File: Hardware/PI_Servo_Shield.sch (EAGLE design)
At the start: 109 parts, among them J1 RASPBERRYPI-40-PIN-GPIO, J19 QWIIC, J20 USB C, J21 Serial, Q1 2N7002PW, Q12 2.5A/30V/105mΩ, Q2 2.5A/30V/105mΩ, Q4 2N7002PW, Q5 2.5A/30V/105mΩ, Q7 2.5A/30V/105mΩ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

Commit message: Added tRestrict around standofs as required by HAT specs
Also moved to correct 2.5 A PTC (1812 package).
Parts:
- F2: value 6V/2A -> 16V/2.5A(5A TRIP); device SparkFun-Fuses:PPTC_6V2A -> SparkFun-Fuses:PPTC_16V_2.5A
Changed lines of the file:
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@@
 <grid distance="0.1" unitdist="inch" unit="inch" style="lines" multiple="1" display="no" altdistance="0.01" altunitdist="inch" altunit="inch"/>
 <layers>
-<layer number="1" name="Top" color="4" fill="1" visible="yes" active="no"/>
-<layer number="2" name="Route2" color="1" fill="3" visible="yes" active="no"/>
-<layer number="3" name="Route3" color="4" fill="3" visible="yes" active="no"/>
-<layer number="4" name="Route4" color="1" fill="4" visible="yes" active="no"/>
-<layer number="5" name="Route5" color="4" fill="4" visible="yes" active="no"/>
-<layer number="6" name="Route6" color="1" fill="8" visible="yes" active="no"/>
-<layer number="7" name="Route7" color="4" fill="8" visible="yes" active="no"/>
-<layer number="8" name="Route8" color="1" fill="2" visible="yes" active="no"/>
-<layer number="9" name="Route9" color="4" fill="2" visible="yes" active="no"/>
-<layer number="10" name="Route10" color="1" fill="7" visible="yes" active="no"/>
-<layer number="11" name="Route11" color="4" fill="7" visible="yes" active="no"/>
-<layer number="12" name="Route12" color="1" fill="5" visible="yes" active="no"/>
-<layer number="13" name="Route13" color="4" fill="5" visible="yes" active="no"/>
-<layer number="14" name="Route14" color="1" fill="6" visible="yes" active="no"/>
-<layer number="15" name="Route15" color="4" fill="6" visible="yes" active="no"/>
-<layer number="16" name="Bottom" color="1" fill="1" visible="yes" active="no"/>
-<layer number="17" name="Pads" color="2" fill="1" visible="yes" active="no"/>
-<layer number="18" name="Vias" color="2" fill="1" visible="yes" active="no"/>
-<layer number="19" name="Unrouted" color="6" fill="1" visible="yes" active="no"/>
-<layer number="20" name="Dimension" color="15" fill="1" visible="yes" active="no"/>
-<layer number="21" name="tPlace" color="16" fill="1" visible="yes" active="no"/>
-<layer number="22" name="bPlace" color="14" fill="1" visible="yes" active="no"/>
-<layer number="23" name="tOrigins" color="15" fill="1" visible="yes" active="no"/>
-<layer number="24" name="bOrigins" color="15" fill="1" visible="yes" active="no"/>
-<layer number="25" name="tNames" color="7" fill="1" visible="yes" active="no"/>
-<layer number="26" name="bNames" color="7" fill="1" visible="yes" active="no"/>
-<layer number="27" name="tValues" color="7" fill="1" visible="yes" active="no"/>
-<layer number="28" name="bValues" color="7" fill="1" visible="yes" active="no"/>
+<layer number="1" name="Top" color="4" fill="1" visible="no" active="no"/>
+<layer number="2" name="Route2" color="1" fill="3" visible="no" active="no"/>
+<layer number="3" name="Route3" color="4" fill="3" visible="no" active="no"/>
+<layer number="4" name="Route4" color="1" fill="4" visible="no" active="no"/>
+<layer number="5" name="Route5" color="4" fill="4" visible="no" active="no"/>
+<layer number="6" name="Route6" color="1" fill="8" visible="no" active="no"/>
+<layer number="7" name="Route7" color="4" fill="8" visible="no" active="no"/>
+<layer number="8" name="Route8" color="1" fill="2" visible="no" active="no"/>
+<layer number="9" name="Route9" color="4" fill="2" visible="no" active="no"/>
+<layer number="10" name="Route10" color="1" fill="7" visible="no" active="no"/>
+<layer number="11" name="Route11" color="4" fill="7" visible="no" active="no"/>
+<layer number="12" name="Route12" color="1" fill="5" visible="no" active="no"/>
+<layer number="13" name="Route13" color="4" fill="5" visible="no" active="no"/>
+<layer number="14" name="Route14" color="1" fill="6" visible="no" active="no"/>
+<layer number="15" name="Route15" color="4" fill="6" visible="no" active="no"/>
+<layer number="16" name="Bottom" color="1" fill="1" visible="no" active="no"/>
+<layer number="17" name="Pads" color="2" fill="1" visible="no" active="no"/>
+<layer number="18" name="Vias" color="2" fill="1" visible="no" active="no"/>
+<layer number="19" name="Unrouted" color="6" fill="1" visible="no" active="no"/>
+<layer number="20" name="Dimension" color="15" fill="1" visible="no" active="no"/>
+<layer number="21" name="tPlace" color="16" fill="1" visible="no" active="no"/>
+<layer number="22" name="bPlace" color="14" fill="1" visible="no" active="no"/>
+<layer number="23" name="tOrigins" color="15" fill="1" visible="no" active="no"/>
+<layer number="24" name="bOrigins" color="15" fill="1" visible="no" active="no"/>
+<layer number="25" name="tNames" color="7" fill="1" visible="no" active="no"/>
+<layer number="26" name="bNames" color="7" fill="1" visible="no" active="no"/>
+<layer number="27" name="tValues" color="7" fill="1" visible="no" active="no"/>
+<layer number="28" name="bValues" color="7" fill="1" visible="no" active="no"/>
 <layer number="29" name="tStop" color="7" fill="3" visible="no" active="no"/>
 <layer number="30" name="bStop" color="7" fill="6" visible="no" active="no"/>
@@
 <layer number="35" name="tGlue" color="7" fill="4" visible="no" active="no"/>
 <layer number="36" name="bGlue" color="7" fill="5" visible="no" active="no"/>
-<layer number="37" name="tTest" color="7" fill="1" visible="yes" active="no"/>
-<layer number="38" name="bTest" color="7" fill="1" visible="yes" active="no"/>
+<layer number="37" name="tTest" color="7" fill="1" visible="no" active="no"/>
+<layer number="38" name="bTest" color="7" fill="1" visible="no" active="no"/>
 <layer number="39" name="tKeepout" color="4" fill="11" visible="no" active="no"/>
 <layer number="40" name="bKeepout" color="1" fill="11" visible="no" active="no"/>
@@
 <layer number="44" name="Drills" color="7" fill="1" visible="no" active="no"/>
 <layer number="45" name="Holes" color="7" fill="1" visible="no" active="no"/>
-<layer number="46" name="Milling" color="3" fill="1" visible="yes" active="no"/>
-<layer number="47" name="Measures" color="7" fill="1" visible="yes" active="no"/>
-<layer number="48" name="Document" color="62" fill="7" visible="yes" active="no"/>
-<layer number="49" name="Reference" color="7" fill="1" visible="yes" active="no"/>
-<layer number="50" name="dxf" color="7" fill="1" visible="yes" active="no"/>
-<layer number="51" name="tDocu" color="6" fill="1" visible="yes" active="no"/>
-<layer number="52" name="bDocu" color="7" fill="1" visible="yes" active="no"/>
-<layer number="53" name="tGND_GNDA" color="7" fill="9" visible="yes" active="no"/>
-<layer number="54" name="bGND_GNDA" color="1" fill="9" visible="yes" active="no"/>
-<layer number="56" name="wert" color="7" fill="1" visible="yes" active="no"/>
-<layer number="57" name="tCAD" color="7" fill="1" visible="yes" active="no"/>
-<layer number="59" name="tCarbon" color="7" fill="1" visible="yes" active="no"/>
-<layer number="60" name="bCarbon" color="7" fill="1" visible="yes" active="no"/>
+<layer number="46" name="Milling" color="3" fill="1" visible="no" active="no"/>
+<layer number="47" name="Measures" color="7" fill="1" visible="no" active="no"/>
+<layer number="48" name="Document" color="62" fill="7" visible="no" active="no"/>
+<layer number="49" name="Reference" color="7" fill="1" visible="no" active="no"/>
+<layer number="50" name="dxf" color="7" fill="1" visible="no" active="no"/>
+<layer number="51" name="tDocu" color="6" fill="1" visible="no" active="no"/>
+<layer number="52" name="bDocu" color="7" fill="1" visible="no" active="no"/>
+<layer number="53" name="tGND_GNDA" color="7" fill="9" visible="no" active="no"/>
+<layer number="54" name="bGND_GNDA" color="1" fill="9" visible="no" active="no"/>
+<layer number="56" name="wert" color="7" fill="1" visible="no" active="no"/>
+<layer number="57" name="tCAD" color="7" fill="1" visible="no" active="no"/>
+<layer number="59" name="tCarbon" color="7" fill="1" visible="no" active="no"/>
+<layer number="60" name="bCarbon" color="7" fill="1" visible="no" active="no"/>
 <layer number="88" name="SimResults" color="9" fill="1" visible="no" active="yes"/>
 <layer number="89" name="SimProbes" color="9" fill="1" visible="no" active="yes"/>
@@
 <part name="GND16" library="SparkFun-PowerSymbols" deviceset="GND" device=""/>
 <part name="JP2" library="SparkFun-Jumpers" deviceset="JUMPER-SMT_2_NO" device="_SILK" value="FUSE BP"/>
-<part name="F2" library="SparkFun-Fuses" deviceset="PPTC" device="_6V2A" value="6V/2A"/>
+<part name="F2" library="SparkFun-Fuses" deviceset="PPTC" device="_16V_2.5A" value="16V/2.5A(5A TRIP)"/>
 <part name="SUPPLY3" library="SparkFun-PowerSymbols" deviceset="VIN" device="" value="USB-5V"/>
 <part name="GND4" library="SparkFun-PowerSymbols" deviceset="GND" device=""/>

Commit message: final stuff during eng check for reds
Schematic cleanup.
Corrected OR Gate in latest library to correct SOT353 (was from older library)
Added PROD_ID to dual PNP (TRAN-14386)
moved some vias around to avoid cutting into silk.
re-routed some "natural bridges" on bottom parts.
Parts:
- removed U4: 7432SE, SparkFun:7432SE
- added U2: SN74LVC1G32DCKR, SparkFun-IC-Logic:7432
- J21: value Serial -> RVR
- Q1, Q4: value 2N7002PW -> 310mA/60V/1.6Ω
- Q12, Q2, Q5, Q7, Q9: value 2.5A/30V/105mΩ -> 20V/4.2A/52mΩ/1.4W; device SparkFun-DiscreteSemi:MOSFET_PCH-DMG2307L -> SparkFun-DiscreteSemi:MOSFET_PCH-DMG2305UX-7
- R17, R18: value 100 -> 240; device SparkFun-Resistors:100OHM-0603-1/4W-5% -> SparkFun-Resistors:240OHM-0603-1/10W-1%
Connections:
- net GND: now also U2G2.P$V-; no longer U4.GND
- net N$17: now also U2G1.Y; no longer U4.Y
- net PI-5V: now also U2G2.P$V+; no longer U4.VCC
- net RVR-5V: now also U2G1.A; no longer U4.A
- net USB-5V: now also U2G1.B; no longer U4.B
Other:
- note added: "(Isolates Pi 5V header from Servo power when USB OR RVR is connected)"
- note added: "Cut this jumper (JP4) to *permanently* Isolate Pi 5V Header from Servo power"
- note added: "Serial UART 4-pin Header"
- note added: "Test points"
- note added: "v12"
- note removed: "Clear this jumper to disconnect servo power from Pi power rail"
- note removed: "Serial Connector"
- note removed: "v11"
- moved on the sheet: C3, C4, C5, C6, C7, C8, Q11Q1, Q11Q2, Q12, R17, R18, R19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

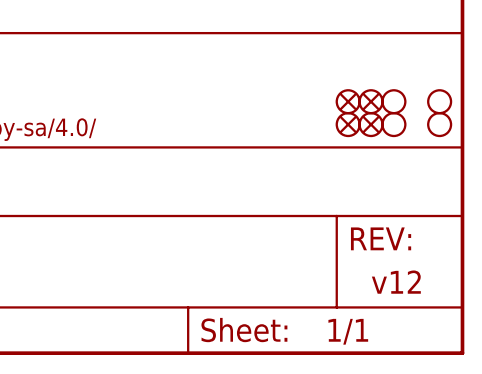
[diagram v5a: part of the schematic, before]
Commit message: qc double-check changes - and SS mods
-bumped version to v20 (was previously v12)
-Moved bottom parts for more clearance from SS route
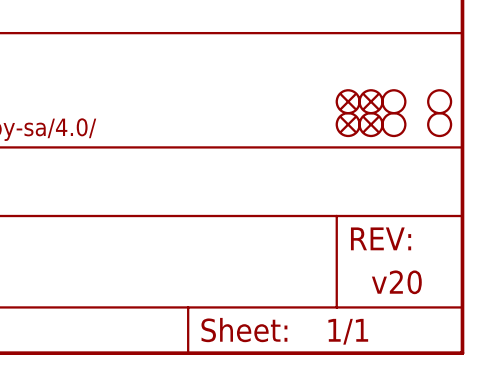
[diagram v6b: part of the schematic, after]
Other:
- note added: "v20"
- note removed: "v12"
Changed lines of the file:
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@@
 <plain>
 <text x="349.758" y="11.43" size="2.54" layer="94" font="vector">M. Hord</text>
-<text x="421.64" y="6.604" size="2.54" layer="94" font="vector" ratio="12">v12</text>
+<text x="421.64" y="6.604" size="2.54" layer="94" font="vector" ratio="12">v20</text>
 <wire x1="0" y1="152.4" x2="139.7" y2="152.4" width="0.3048" layer="97" style="longdash"/>
 <wire x1="139.7" y1="152.4" x2="139.7" y2="0" width="0.3048" layer="97" style="longdash"/>

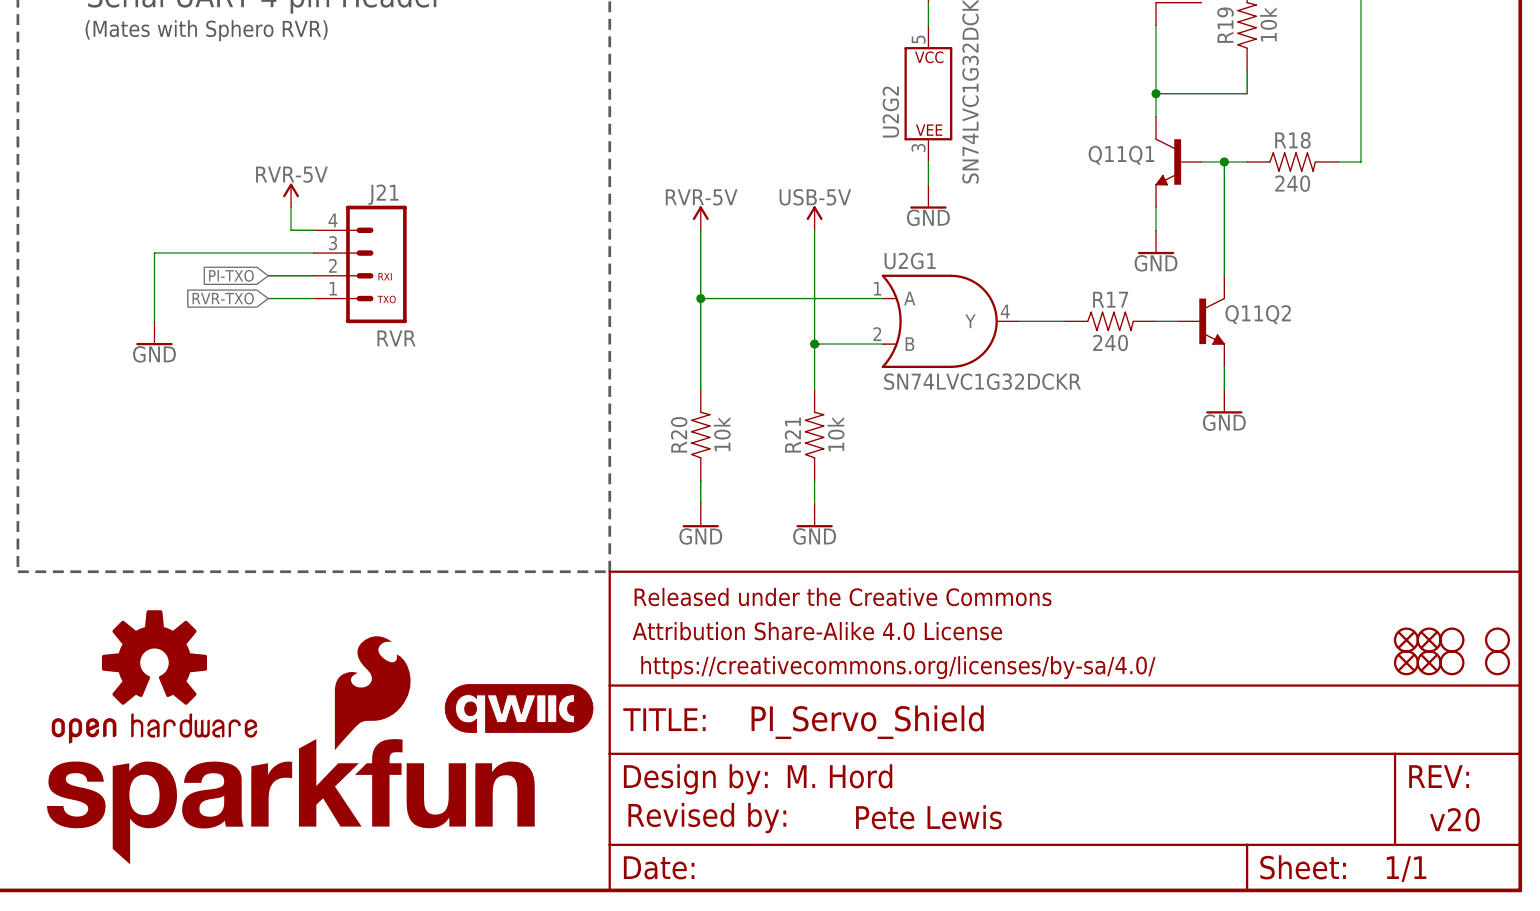
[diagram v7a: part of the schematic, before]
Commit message: Fixed RX/TX on RVR 4-pin header
-swapped rx/tx lines on the RVR header.

-updated board buzzard labels on the header to reflect correction (and note, they are labeled in relation to the raspi)

-bumped version to v21 in brd and sch

-added RVR pin names in schematic next to 4-pin header. Put it on info layer. Just there to clarify what those pins are (in relation to the RVR).

-moved test point (TP23) 0.05 inch east/right to gain more clarance from nearby bottom resistor (R13).
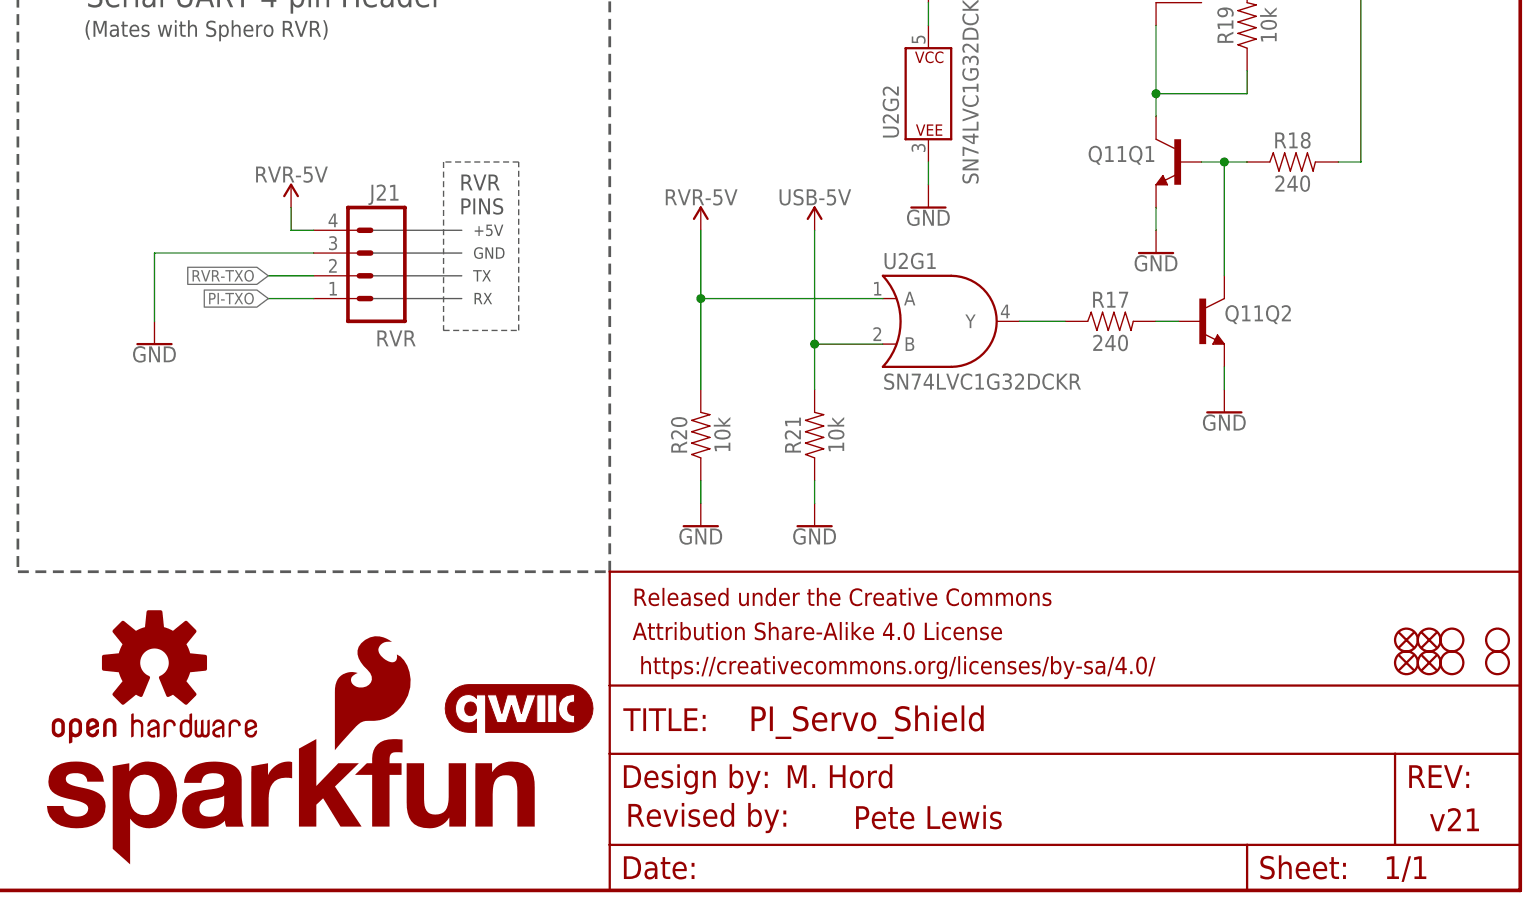
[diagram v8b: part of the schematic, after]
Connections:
- net PI-TXO: now also J21.1; no longer J21.2
- net RVR-TXO: now also J21.2; no longer J21.1
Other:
- note added: "+5V"
- note added: "GND"
- note added: "RVR PINS"
- note added: "RX"
- note added: "TX"
- note added: "v21"
- note removed: "RXI"
- note removed: "TXO"
- note removed: "v20"
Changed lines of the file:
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@@
 <?xml version="1.0" encoding="utf-8"?>
 <!DOCTYPE eagle SYSTEM "eagle.dtd">
-<eagle version="9.2.2">
+<eagle version="9.4.0">
 <drawing>
 <settings>
@@
 <plain>
 <text x="349.758" y="11.43" size="2.54" layer="94" font="vector">M. Hord</text>
-<text x="421.64" y="6.604" size="2.54" layer="94" font="vector" ratio="12">v20</text>
+<text x="421.64" y="6.604" size="2.54" layer="94" font="vector" ratio="12">v21</text>
 <wire x1="0" y1="152.4" x2="139.7" y2="152.4" width="0.3048" layer="97" style="longdash"/>
 <wire x1="139.7" y1="152.4" x2="139.7" y2="0" width="0.3048" layer="97" style="longdash"/>
@@
 <wire x1="381" y1="200.66" x2="419.1" y2="200.66" width="0.3048" layer="97" style="shortdash"/>
 <wire x1="381" y1="139.7" x2="381" y2="200.66" width="0.3048" layer="97" style="shortdash"/>
-<text x="304.292" y="65.532" size="0.8128" layer="94" font="vector">TXO</text>
-<text x="304.292" y="68.072" size="0.8128" layer="94" font="vector">RXI</text>
 <text x="213.36" y="101.6" size="1.778" layer="97" font="vector">Serial Swtich</text>
 <text x="213.36" y="99.568" size="1.778" layer="97" font="vector" align="top-left">Selects which TX source
@@
 <text x="146.05" y="42.418" size="2.54" layer="97" font="vector">Test points</text>
 <wire x1="282.702" y1="242.062" x2="289.56" y2="254" width="0.1524" layer="97" style="shortdash"/>
+<text x="313.436" y="75.438" size="1.778" layer="97" font="vector">RVR
+PINS</text>
+<text x="314.96" y="73.66" size="1.27" layer="97" font="vector" ratio="12" align="center-left">+5V</text>
+<text x="314.96" y="71.12" size="1.27" layer="97" font="vector" ratio="12" align="center-left">GND</text>
+<text x="314.96" y="68.58" size="1.27" layer="97" font="vector" ratio="12" align="center-left">TX</text>
+<text x="314.96" y="66.04" size="1.27" layer="97" font="vector" ratio="12" align="center-left">RX</text>
+<wire x1="303.784" y1="66.04" x2="313.69" y2="66.04" width="0.1524" layer="97"/>
+<wire x1="303.784" y1="68.58" x2="313.69" y2="68.58" width="0.1524" layer="97"/>
+<wire x1="303.784" y1="71.12" x2="313.69" y2="71.12" width="0.1524" layer="97"/>
+<wire x1="303.784" y1="73.66" x2="313.69" y2="73.66" width="0.1524" layer="97"/>
+<wire x1="311.658" y1="81.28" x2="311.658" y2="62.484" width="0.1524" layer="97" style="shortdash"/>
+<wire x1="311.658" y1="62.484" x2="320.04" y2="62.484" width="0.1524" layer="97" style="shortdash"/>
+<wire x1="320.04" y1="62.484" x2="320.04" y2="81.28" width="0.1524" layer="97" style="shortdash"/>
+<wire x1="320.04" y1="81.28" x2="311.658" y2="81.28" width="0.1524" layer="97" style="shortdash"/>
 </plain>
 <instances>
@@
 </segment>
 <segment>
-<wire x1="297.18" y1="68.58" x2="292.1" y2="68.58" width="0.1524" layer="91"/>
-<label x="292.1" y="68.58" size="1.27" layer="95" font="vector" rot="MR0" xref="yes"/>
-<pinref part="J21" gate="J1" pin="2"/>
-</segment>
-<segment>
 <pinref part="TP20" gate="G$1" pin="1"/>
 <wire x1="187.96" y1="25.4" x2="185.42" y2="25.4" width="0.1524" layer="91"/>
 <label x="185.42" y="25.4" size="1.27" layer="95" font="vector" rot="R180" xref="yes"/>
+</segment>
+<segment>
+<wire x1="297.18" y1="66.04" x2="292.1" y2="66.04" width="0.1524" layer="91"/>
+<label x="292.1" y="66.04" size="1.27" layer="95" font="vector" rot="MR0" xref="yes"/>
+<pinref part="J21" gate="J1" pin="1"/>
 </segment>
 </net>
@@
 <net name="RVR-TXO" class="0">
 <segment>
-<wire x1="297.18" y1="66.04" x2="292.1" y2="66.04" width="0.1524" layer="91"/>
-<label x="292.1" y="66.04" size="1.27" layer="95" font="vector" rot="MR0" xref="yes"/>
-<pinref part="J21" gate="J1" pin="1"/>
-</segment>
-<segment>
 <pinref part="TP21" gate="G$1" pin="1"/>
 <wire x1="187.96" y1="22.86" x2="185.42" y2="22.86" width="0.1524" layer="91"/>
@@
 <pinref part="S1" gate="1" pin="S"/>
 </segment>
-</net>
+<segment>
+<wire x1="297.18" y1="68.58" x2="292.1" y2="68.58" width="0.1524" layer="91"/>
+<label x="292.1" y="68.58" size="1.27" layer="95" font="vector" rot="MR0" xref="yes"/>
+<pinref part="J21" gate="J1" pin="2"/>
+</segment>
+</net>
